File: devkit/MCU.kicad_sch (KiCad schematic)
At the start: 38 parts, among them IC601 FAN5622SX, IC602 USBLC6-2P6, IC603 MX25U51245GZ4I00, IC604 NTS0104GU12, J601 Jumper, J602 Jumper, J603 Jumper, J604 Jumper, M601 NORA-B106, X601 DEBUG, X602 Current, X603 Device, X604 UART, X605 GPIO, X606 Current, X607 IO Current, X608 Display, X609 Current, X610 LED Current

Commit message: Bug: Issue #185
- Set all solder jumpers to not assembled and remove them from BOM
Closes #185

Signed-off-by: Daniel Kampert <DanielKampert@kampis-elektroecke.de>
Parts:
- JP601, JP602, JP603, JP604, JP605: now left out of the parts list
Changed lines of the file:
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@@
 		(unit 1)
 		(exclude_from_sim no)
-		(in_bom yes)
+		(in_bom no)
 		(on_board yes)
 		(dnp no)
@@
 		(unit 1)
 		(exclude_from_sim no)
-		(in_bom yes)
+		(in_bom no)
 		(on_board yes)
 		(dnp no)
@@
 		(unit 1)
 		(exclude_from_sim no)
-		(in_bom yes)
+		(in_bom no)
 		(on_board yes)
 		(dnp no)
@@
 		(unit 1)
 		(exclude_from_sim no)
-		(in_bom yes)
+		(in_bom no)
 		(on_board yes)
 		(dnp no)
@@
 		(unit 1)
 		(exclude_from_sim no)
-		(in_bom yes)
+		(in_bom no)
 		(on_board yes)
 		(dnp no)

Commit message: Revert "Bug: Issue #185"
This reverts commit 3b9bfdeb6c5eb0a24956d5269e31e46a928e9a1e.
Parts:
- JP601, JP602, JP603, JP604, JP605: now in the parts list
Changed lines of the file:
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@@
 		(unit 1)
 		(exclude_from_sim no)
-		(in_bom no)
+		(in_bom yes)
 		(on_board yes)
 		(dnp no)
@@
 		(unit 1)
 		(exclude_from_sim no)
-		(in_bom no)
+		(in_bom yes)
 		(on_board yes)
 		(dnp no)
@@
 		(unit 1)
 		(exclude_from_sim no)
-		(in_bom no)
+		(in_bom yes)
 		(on_board yes)
 		(dnp no)
@@
 		(unit 1)
 		(exclude_from_sim no)
-		(in_bom no)
+		(in_bom yes)
 		(on_board yes)
 		(dnp no)
@@
 		(unit 1)
 		(exclude_from_sim no)
-		(in_bom no)
+		(in_bom yes)
 		(on_board yes)
 		(dnp no)

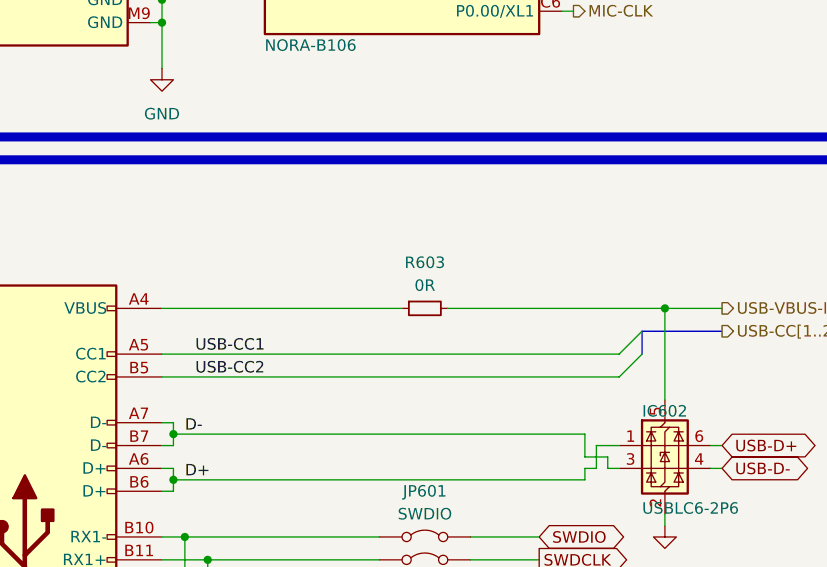
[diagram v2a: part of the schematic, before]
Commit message: Revert "Feature: Issue #184"
This reverts commit f0a18e2688c143ce39ba7e204db2730629a8a8a3.
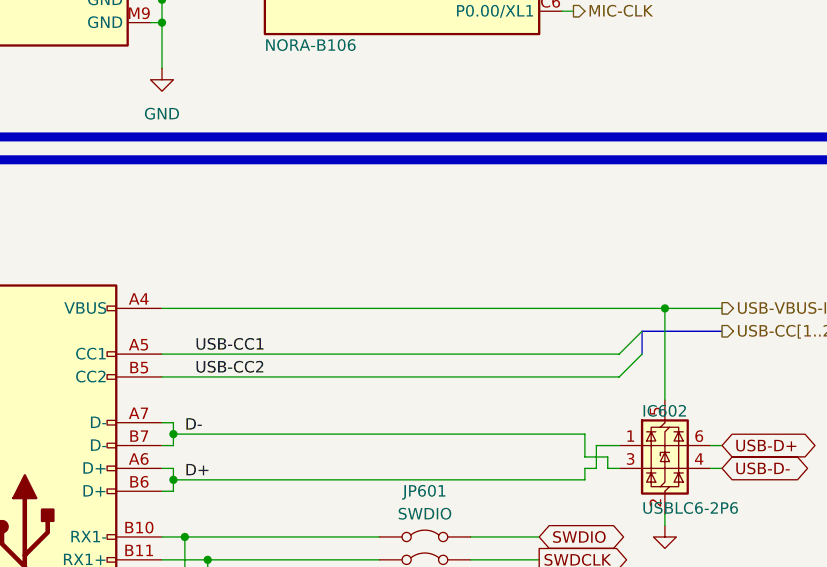
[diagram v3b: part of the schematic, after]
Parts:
- removed R603: 0R, Resistor_SMD:R_0805_2012Metric, symbol Device:R_Small
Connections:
- net USB-VBUS-In: now also X603.A4 (VBUS), X603.A9 (VBUS), X603.B4 (VBUS), X603.B9 (VBUS)
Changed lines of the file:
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@@
 	(wire
 		(pts
-			(xy 109.22 173.99) (xy 135.89 173.99)
+			(xy 109.22 173.99) (xy 165.1 173.99)
 		)
 		(stroke
@@
 	(wire
 		(pts
-			(xy 140.97 173.99) (xy 165.1 173.99)
-		)
-		(stroke
-			(width 0)
-			(type default)
-		)
-	)
-	(wire
-		(pts
 			(xy 347.98 36.83) (xy 347.98 39.37)
 		)
@@
 					(unit 1)
 				)
-			)
-		)
-	)
-	(symbol
-		(lib_id "Device:R_Small")
-		(at 138.43 173.99 90)
-		(mirror x)
-		(unit 1)
-		(exclude_from_sim no)
-		(in_bom yes)
-		(on_board yes)
-		(dnp no)
-		(fields_autoplaced yes)
-		(property "Reference" "R603"
-			(at 138.43 168.91 90)
-			(effects
-				(font
-					(size 1.27 1.27)
-				)
-			)
-		)
-		(property "Value" "0R"
-			(at 138.43 171.45 90)
-			(effects
-				(font
-					(size 1.27 1.27)
-				)
-			)
-		)
-		(property "Footprint" "Resistor_SMD:R_0805_2012Metric"
-			(at 138.43 173.99 0)
-			(effects
-				(font
-					(size 1.27 1.27)
-				)
-				(hide yes)
-			)
-		)
-		(property "Datasheet" "https://www.mouser.de/datasheet/3/40/1/cr.pdf"
-			(at 138.43 173.99 0)
-			(effects
-				(font
-					(size 1.27 1.27)
-				)
-				(hide yes)
-			)
-		)
-		(property "Description" "Resistor, small symbol"
-			(at 138.43 173.99 0)
-			(effects
-				(font
-					(size 1.27 1.27)
-				)
-				(hide yes)
-			)
-		)
-		(property "CONFIG" ""
-			(at 138.43 173.99 0)
-			(effects
-				(font
-					(size 1.27 1.27)
-				)
-				(hide yes)
-			)
-		)
-		(property "manf" "Bourns"
-			(at 138.43 173.99 0)
-			(effects
-				(font
-					(size 1.27 1.27)
-				)
-				(hide yes)
-			)
-		)
-		(property "manf#" "CR0805-J/-000ELF"
-			(at 138.43 173.99 0)
-			(effects
-				(font
-					(size 1.27 1.27)
-				)
-				(hide yes)
-			)
-		)
-		(property "mouser#" "652-CR0805-J/-000ELF"
-			(at 138.43 173.99 0)
-			(effects
-				(font
-					(size 1.27 1.27)
-				)
-				(hide yes)
-			)
-		)
-		(pin "1"
-		)
-		(pin "2"
-		)
-		(instances
-			(project "ZSWatch-Watch-DevKit"
-				(path "/d5742f03-3b1a-42e5-a384-018bd4b919aa/c5103ceb-5325-4a84-a025-9638a412984e/8c9f2ee7-84da-4a9a-b0dc-117e0b0a9ea7"
-					(reference "R603")
-					(unit 1)
-				)

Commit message: Feature: Issue #184
- Add 0R to disconnect VBUS from the USB connector
- Add bridge to remove VBUS from nPM1300

Closes #184

Signed-off-by: Daniel Kampert <DanielKampert@kampis-elektroecke.de>
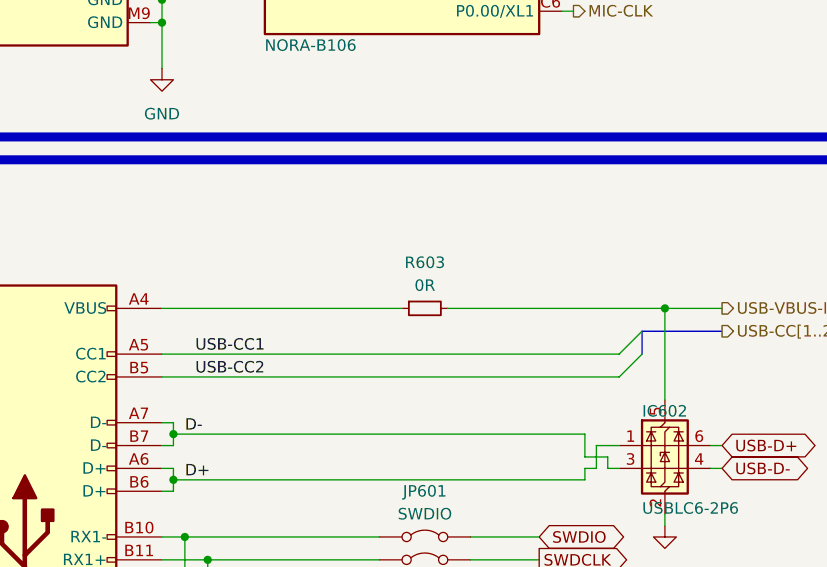
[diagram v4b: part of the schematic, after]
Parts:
- added R603: 0R, Resistor_SMD:R_0805_2012Metric, symbol Device:R_Small
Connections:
- net USB-VBUS-In: now also R603.2; no longer X603.A4 (VBUS), X603.A9 (VBUS), X603.B4 (VBUS), X603.B9 (VBUS)
- new net: R603.1, X603.A4 (VBUS), X603.A9 (VBUS), X603.B4 (VBUS), X603.B9 (VBUS)
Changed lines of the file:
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@@
 	(wire
 		(pts
-			(xy 109.22 173.99) (xy 165.1 173.99)
+			(xy 109.22 173.99) (xy 135.89 173.99)
 		)
 		(stroke
@@
 	(wire
 		(pts
+			(xy 140.97 173.99) (xy 165.1 173.99)
+		)
+		(stroke
+			(width 0)
+			(type default)
+		)
+	)
+	(wire
+		(pts
 			(xy 347.98 36.83) (xy 347.98 39.37)
 		)
@@
 					(unit 1)
 				)
+			)
+		)
+	)
+	(symbol
+		(lib_id "Device:R_Small")
+		(at 138.43 173.99 90)
+		(mirror x)
+		(unit 1)
+		(exclude_from_sim no)
+		(in_bom yes)
+		(on_board yes)
+		(dnp no)
+		(fields_autoplaced yes)
+		(property "Reference" "R603"
+			(at 138.43 168.91 90)
+			(effects
+				(font
+					(size 1.27 1.27)
+				)
+			)
+		)
+		(property "Value" "0R"
+			(at 138.43 171.45 90)
+			(effects
+				(font
+					(size 1.27 1.27)
+				)
+			)
+		)
+		(property "Footprint" "Resistor_SMD:R_0805_2012Metric"
+			(at 138.43 173.99 0)
+			(effects
+				(font
+					(size 1.27 1.27)
+				)
+				(hide yes)
+			)
+		)
+		(property "Datasheet" "https://www.mouser.de/datasheet/3/40/1/cr.pdf"
+			(at 138.43 173.99 0)
+			(effects
+				(font
+					(size 1.27 1.27)
+				)
+				(hide yes)
+			)
+		)
+		(property "Description" "Resistor, small symbol"
+			(at 138.43 173.99 0)
+			(effects
+				(font
+					(size 1.27 1.27)
+				)
+				(hide yes)
+			)
+		)
+		(property "CONFIG" ""
+			(at 138.43 173.99 0)
+			(effects
+				(font
+					(size 1.27 1.27)
+				)
+				(hide yes)
+			)
+		)
+		(property "manf" "Bourns"
+			(at 138.43 173.99 0)
+			(effects
+				(font
+					(size 1.27 1.27)
+				)
+				(hide yes)
+			)
+		)
+		(property "manf#" "CR0805-J/-000ELF"
+			(at 138.43 173.99 0)
+			(effects
+				(font
+					(size 1.27 1.27)
+				)
+				(hide yes)
+			)
+		)
+		(property "mouser#" "652-CR0805-J/-000ELF"
+			(at 138.43 173.99 0)
+			(effects
+				(font
+					(size 1.27 1.27)
+				)
+				(hide yes)
+			)
+		)
+		(pin "1"
+		)
+		(pin "2"
+		)
+		(instances
+			(project "ZSWatch-Watch-DevKit"
+				(path "/d5742f03-3b1a-42e5-a384-018bd4b919aa/c5103ceb-5325-4a84-a025-9638a412984e/8c9f2ee7-84da-4a9a-b0dc-117e0b0a9ea7"
+					(reference "R603")
+					(unit 1)
+				)
